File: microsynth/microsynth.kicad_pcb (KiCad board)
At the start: 2 copper layers, 365.8 x 153.7 mm, 271 parts, among them J1 AudioJack3, J2 Conn_01x03_Male, J3 Conn_01x04_Male, J4 Conn_01x04_Male, J5 Conn_01x02_Male, J8 AudioJack2, Q1 BC182, Q2 BC182L, Q3 BC548, Q4 BC212 PNP, Q5 BC212 PNP, Q6 BC548, Q7 BC548, Q8 BC548, Q9 BC548, SW1 DRIFT, SW10 SW_SPST, SW11 SW_SPDT, SW12 SOURCE, SW13 THUMBWEEL, SW14 SW_SPDT, SW15 SW_SPDT, SW16 SW_SPDT, SW17 SW_SPDT, SW18-ENV-TO-VCF1 SW_SPDT, SW19-ENV-TO-VCO1 SW_SPDT, SW2 RANGE, SW20-ENV-TO-KEYB1 SW_SPDT, SW21 SW_Rotary2x6, SW22 SW_SPST, SW3 SW_DPTT_SELECTOR, SW4 SW_DPTT_SELECTOR, SW5 SW_SPDT, SW6 SW_DPTT_SELECTOR, SW7 SW_SPDT, SW8 SUSTAIN, SW9 TRIGGER, U1 RC4136, U10 LM741, U11 LM741, U12 LM741, U13 LM741, U14 4016, U15 LF355, U16 LM741, U17 LM741, U18 LM741, U19 LM741, U2 TL072, U20 LM13600, U21 CA3080, U22 4013, U23 LM380N, U3 4011, U4 4016, U5 LF347, U6 TL071, U7 LM741, U8 4001, U9 LM741

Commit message: Replace dodgy parts 1458, 4136 & LF351s
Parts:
- U15: value LF355 -> LF351
- U2: value TL072 -> LM1458
- U20: footprint Package_DIP:DIP-16_W7.62mm -> Package_DIP:DIP-16_W7.62mm_LongPads
- U23: footprint Package_DIP:DIP-14_W7.62mm -> Package_DIP:DIP-14_W7.62mm_LongPads
- U6: value TL071 -> LF351
- moved U5 0.13 mm to (183.4, 126.3)
- moved U1 0.05 mm to (39.4, 133.7)
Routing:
- net -15V: track 1305.9 -> 1309.1 mm
- net Net-(R110-Pad1): track 47.4 -> 48.7 mm
- net Net-(C22-Pad1): track 16.5 -> 17.5 mm
- net GND: track 1073.9 -> 1074.8 mm
- net Net-(C31-Pad1): track 21.8 -> 22.4 mm
- net +15V: track 1422.2 -> 1422.8 mm

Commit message: Proper mounting holes
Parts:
- removed ? (x2): SolderWirePad_1x01_Drill1.2mm, Connector_Wire:SolderWirePad_1x01_Drill1.2mm
- removed REF** (x6): MountingHole_3.2mm_M3, MountingHole:MountingHole_3.2mm_M3
- added H1: MountingHole, MountingHole:MountingHole_3.2mm_M3, F.Cu at (38.1, 90.2)
- added H2: MountingHole, MountingHole:MountingHole_3.2mm_M3, F.Cu at (38.1, 236.2)
- added H3: MountingHole, MountingHole:MountingHole_3.2mm_M3, F.Cu at (210.8, 90.2)
- added H4: MountingHole, MountingHole:MountingHole_3.2mm_M3, F.Cu at (210.8, 236.2)
- added H5: MountingHole, MountingHole:MountingHole_3.2mm_M3, F.Cu at (383.5, 90.2)
- added H6: MountingHole, MountingHole:MountingHole_3.2mm_M3, F.Cu at (383.5, 236.2)
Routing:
- net Net-(R77-Pad2): track 406.5 -> 407.1 mm

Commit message: Replace DP3T footprint, proper wire pads
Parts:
- added H7: MountingHole_Pad, Connector_PinHeader_2.54mm:PinHeader_1x01_P2.54mm_Vertical, B.Cu at (51.1, 233.0)
- added H8: MountingHole_Pad, Connector_PinHeader_2.54mm:PinHeader_1x01_P2.54mm_Vertical, F.Cu at (126.6, 125.2)
- SW12, SW13, SW3, SW4, SW6, SW8, SW9: footprint Buttons_Switches_ThroughHole:G-1128S-1110 -> microsynth:G-1128S-1110
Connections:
- net +15V renamed +VSW
- net -15V renamed -VSW
- SW1 pad 2: Net-(C1-Pad1) -> Net-(H7-Pad1)
- SW1 pad 3: Net-(C1-Pad1) -> Net-(H7-Pad1)
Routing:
- net Net-(C1-Pad1): track 79.0 -> 65.0 mm
- net Net-(H7-Pad1): track 0.00 -> 13.9 mm
- net Net-(C4-Pad1): track 300.0 -> 306.8 mm
- net Net-(SW21-Pad14): track 349.8 -> 356.1 mm
- net S5_VCO2: track 323.1 -> 329.3 mm
- net TO_VCA_C26: track 354.1 -> 359.5 mm
- net Net-(RV27-Pad2): track 117.9 -> 113.3 mm
- net Net-(R133-Pad1): track 304.3 -> 301.0 mm
- net Net-(RV27-Pad3): track 95.8 -> 99.0 mm
- net Net-(C7-Pad1): track 451.4 -> 454.3 mm
- net Net-(SW9-Pad1): track 299.3 -> 302.1 mm
- net Net-(R140-Pad2): track 227.1 -> 229.9 mm
- net TO_VCF_IC20_3: track 407.7 -> 410.5 mm
- net Net-(R61-Pad2): track 217.3 -> 215.3 mm
- net Net-(C17-Pad1): track 274.5 -> 275.5 mm
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
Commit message: Replace all switches with tayda footprint
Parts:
- SW10, SW11, SW14, SW15, SW16, SW17, SW18-ENV-TO-VCF1, SW19-ENV-TO-VCO1, SW20-ENV-TO-KEYB1, SW5, SW7: footprint Buttons_Switches_ThroughHole:GF-624-6014 -> microsynth:11-SS-22-701C
- SW12, SW13, SW3, SW4, SW6, SW8, SW9: footprint microsynth:G-1128S-1110 -> microsynth:11-SS-23-832C
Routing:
- net Net-(RV22-Pad1): track 18.6 -> 23.3 mm
- net KEYBOARD_IC7_PIN_6: track 437.0 -> 441.3 mm
- net S5_VCO2: track 329.3 -> 325.2 mm
- net Net-(R61-Pad2): track 215.3 -> 211.9 mm
- net Net-(R118-Pad1): track 21.1 -> 18.5 mm
- net TO_R41: track 12.8 -> 15.3 mm
- net Net-(C11-Pad1): track 89.1 -> 86.8 mm
- net TO_VCF_IC20_3: track 410.5 -> 412.4 mm
- net Net-(D8-Pad1): track 198.3 -> 196.4 mm
- net Net-(C17-Pad1): track 275.5 -> 277.4 mm
- net VCF_OUT: track 27.0 -> 28.5 mm
- net LFO_MOD_S16: track 14.1 -> 15.6 mm
- net Net-(R111-Pad2): track 90.2 -> 91.5 mm
- net LFO_TO_VR20_SLIDER: track 505.1 -> 503.9 mm
- net VCO2_MOD_SWITCH_S6-1: track 128.6 -> 127.5 mm
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
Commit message: Consolidate switches
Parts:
- added R153: 1k, Resistor_THT:R_Axial_DIN0207_L6.3mm_D2.5mm_P10.16mm_Horizontal, F.Cu at (297.7, 178.6)
- added R154: 100k, Resistor_THT:R_Axial_DIN0207_L6.3mm_D2.5mm_P10.16mm_Horizontal, F.Cu at (247.3, 187.5)
- H8: moved to B.Cu
- SW1: value DRIFT -> SW_DP3T; footprint Buttons_Switches_ThroughHole:G-1128S-1110 -> microsynth:11-SS-23-832C
- SW12: value SOURCE -> SW_DP3T
- SW13: value THUMBWEEL -> SW_DP3T
- SW2: value RANGE -> SW_Rotary2x6
- SW21: footprint Button_Switch_THT:SR2612F-0304-18R0B-D8-N -> microsynth:SR2612F-0304-18R0B-D8-N
- SW3, SW4, SW6: value SW_DPTT_SELECTOR -> SW_DP3T
- SW8: value SUSTAIN -> SW_DP3T
- SW9: value TRIGGER -> SW_DP3T
- renumbered SW18-ENV-TO-VCF1 to SW18, SW19-ENV-TO-VCO1 to SW19, SW20-ENV-TO-KEYB1 to SW20
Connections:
- SW8 pad 7: +VSW -> Net-(R154-Pad2)
- SW9 pad 2: +VSW -> Net-(R153-Pad2)
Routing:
- net +VSW: track 1422.8 -> 1365.2 mm
- net Net-(R153-Pad2): track 0.00 -> 18.5 mm
- net Net-(R154-Pad2): track 0.00 -> 14.5 mm
- net TO_VCO1_R79: track 202.5 -> 198.1 mm

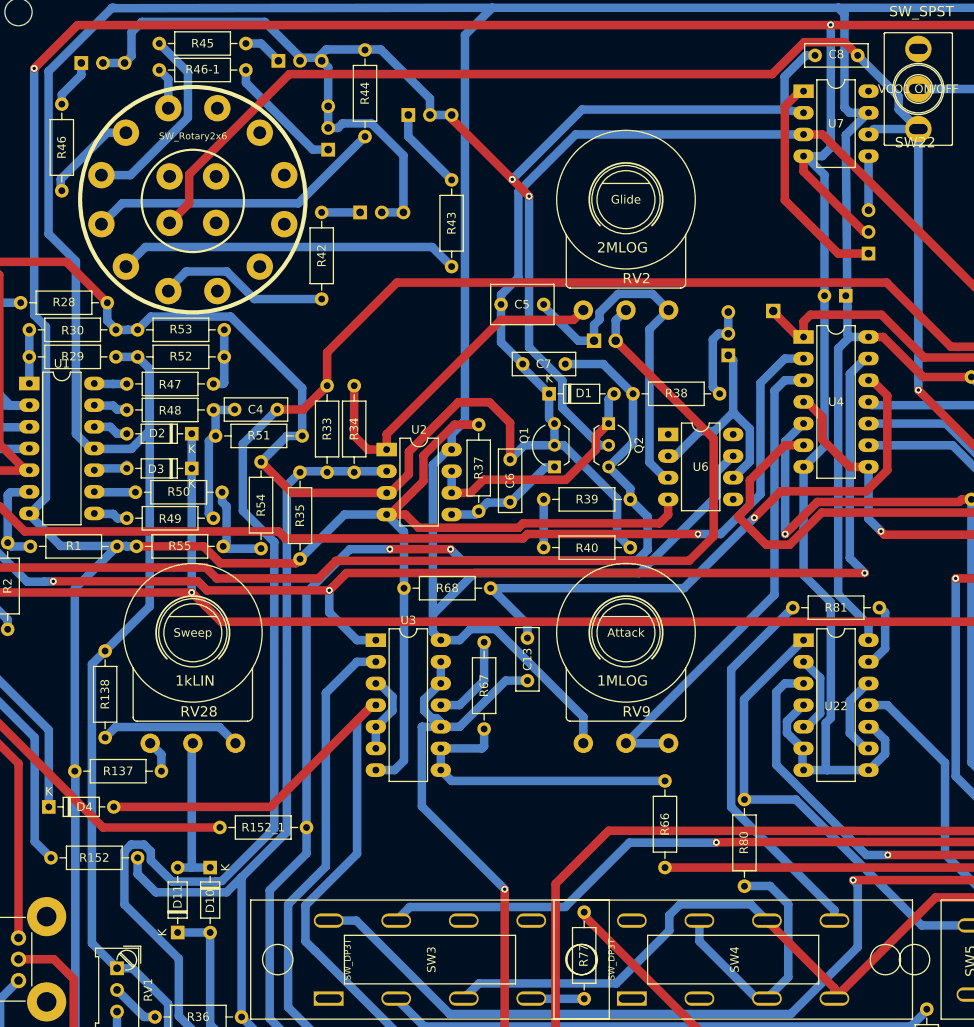
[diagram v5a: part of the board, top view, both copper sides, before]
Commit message: Consolidate all(?) switches
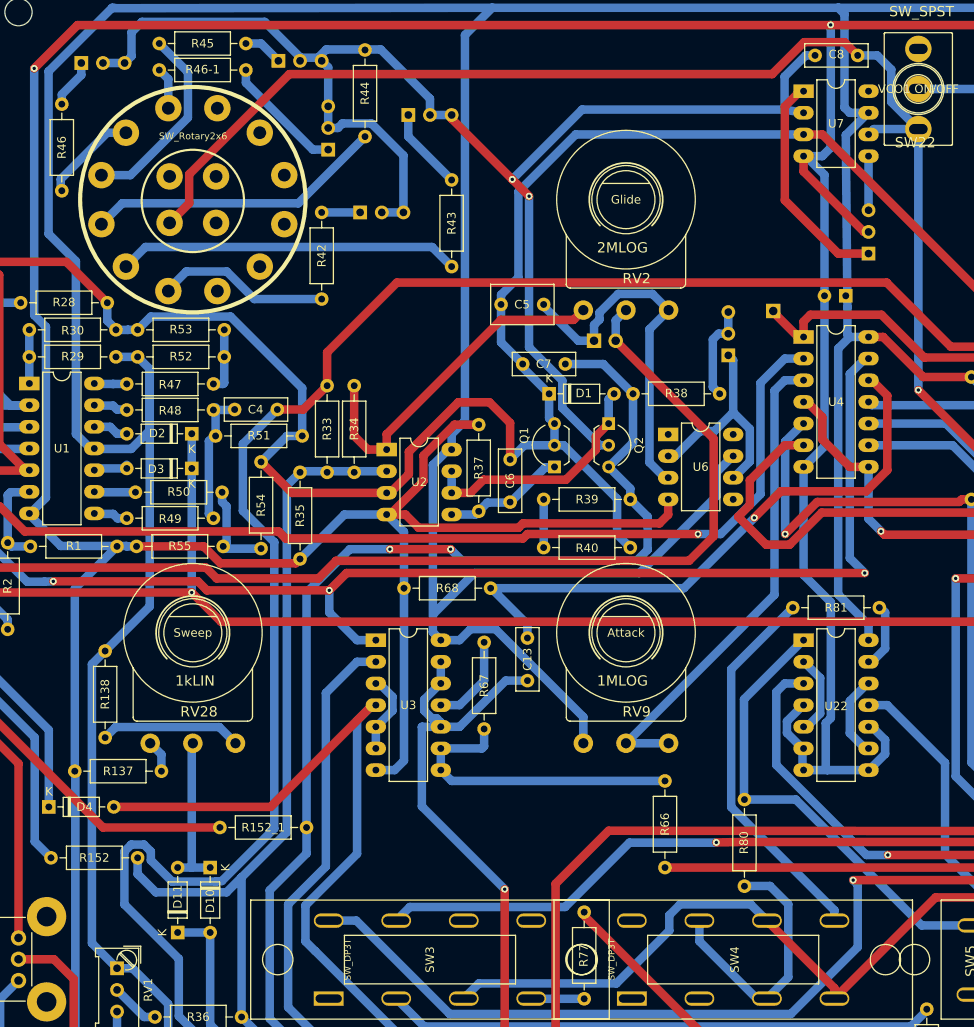
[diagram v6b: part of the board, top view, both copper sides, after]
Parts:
- RV10, RV12, RV14, RV16, RV18, RV2, RV20, RV21, RV23, RV24, RV28, RV9: footprint 4ms_Potentiometer:Pot_16mm_NoDet_RV16AF-4A -> microsynth:Pot_16mm_NoDet_RV16AF-4A
- SW2: footprint MyKi_TH_Panel_Controls:SW_Rotary4+12 -> microsynth:SW_Rotary4+12
- SW22: footprint 4ms:SPDT_KIT -> microsynth:SPDT_KIT
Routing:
- net KEYBOARD_IC7_PIN_6: track 441.3 -> 442.6 mm

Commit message: Update tayda rotary switch footprints and layout
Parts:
- SW10: value SW_SPST -> SW_SPDT
- SW2: footprint microsynth:SW_Rotary4+12 -> microsynth:SR2511F-0206-(L)K0A-C9-S-3
- SW21: footprint microsynth:SR2612F-0304-18R0B-D8-N -> microsynth:SR2511F-0204-(L)K0A-C9-S-3
- moved RV14 0.23 mm to (160.0, 112.2)
- moved R69 0.20 mm to (215.7, 209.5)
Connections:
- SW2 pad 1: Net-(R42-Pad2) -> (no net)
- SW2 pad 10: (no net) -> Net-(R45-Pad2)
- SW2 pad 11: (no net) -> Net-(R46-Pad1)
- SW2 pad 12: (no net) -> Net-(R46-1-Pad1)
- SW2 pad 13: KEYBOARD_IC7_PIN_6 -> (no net)
- SW2 pad 14: (no net) -> KEYBOARD_IC7_PIN_6
- SW2 pad 2: Net-(R43-Pad2) -> (no net)
- SW2 pad 3: Net-(R44-Pad2) -> (no net)
- SW2 pad 4: Net-(R45-Pad2) -> (no net)
- SW2 pad 5: Net-(R46-Pad1) -> (no net)
- SW2 pad 6: Net-(R46-1-Pad1) -> (no net)
- SW2 pad 7: (no net) -> Net-(R42-Pad2)
- SW2 pad 8: (no net) -> Net-(R43-Pad2)
- SW2 pad 9: (no net) -> Net-(R44-Pad2)
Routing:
- net Net-(SW21-Pad14): track 355.0 -> 277.8 mm
- net TO_VCF_R120: track 51.7 -> 38.1 mm
- net Net-(R42-Pad2): track 20.4 -> 9.79 mm
- net Net-(R46-1-Pad1): track 4.92 -> 15.0 mm
- net TO_VCA_C27: track 252.2 -> 242.4 mm
- net Net-(R43-Pad2): track 40.1 -> 31.6 mm
- net Net-(R45-Pad2): track 23.0 -> 29.8 mm
- net Net-(R77-Pad2): track 408.1 -> 414.1 mm
- net VCO2_SAW: track 109.4 -> 115.3 mm
- net Net-(R44-Pad2): track 35.3 -> 30.2 mm
- net Net-(R46-Pad1): track 11.1 -> 7.08 mm
- net VCO2_SQR: track 60.4 -> 56.6 mm
- net Net-(RV20-Pad3): track 72.6 -> 69.2 mm
- net TO_D4: track 216.2 -> 219.5 mm
- net Net-(SW9-Pad1): track 302.1 -> 299.0 mm
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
